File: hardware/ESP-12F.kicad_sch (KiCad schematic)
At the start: 30 parts, among them J10 PROG_PORT, U10 ESP-12F, U11 MCP2558FD-xMF, U8 PI4IOE5V6416LEX, U9 PI4IOE5V6416LEX

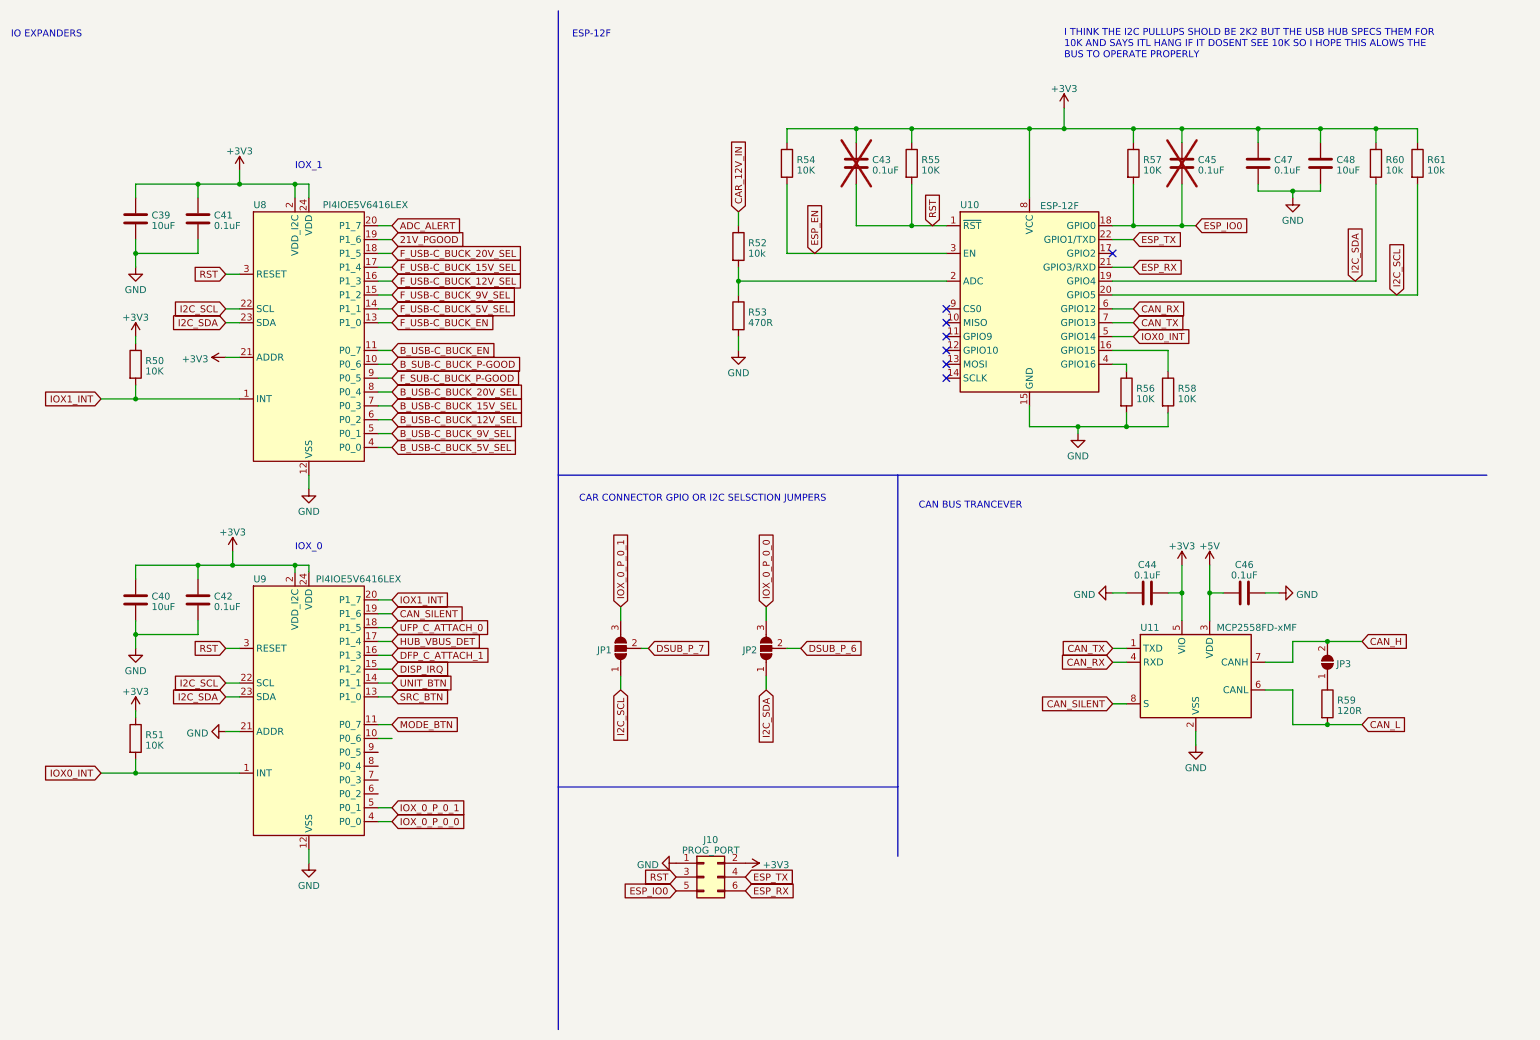
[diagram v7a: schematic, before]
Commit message: working on routing still  finnished psu section
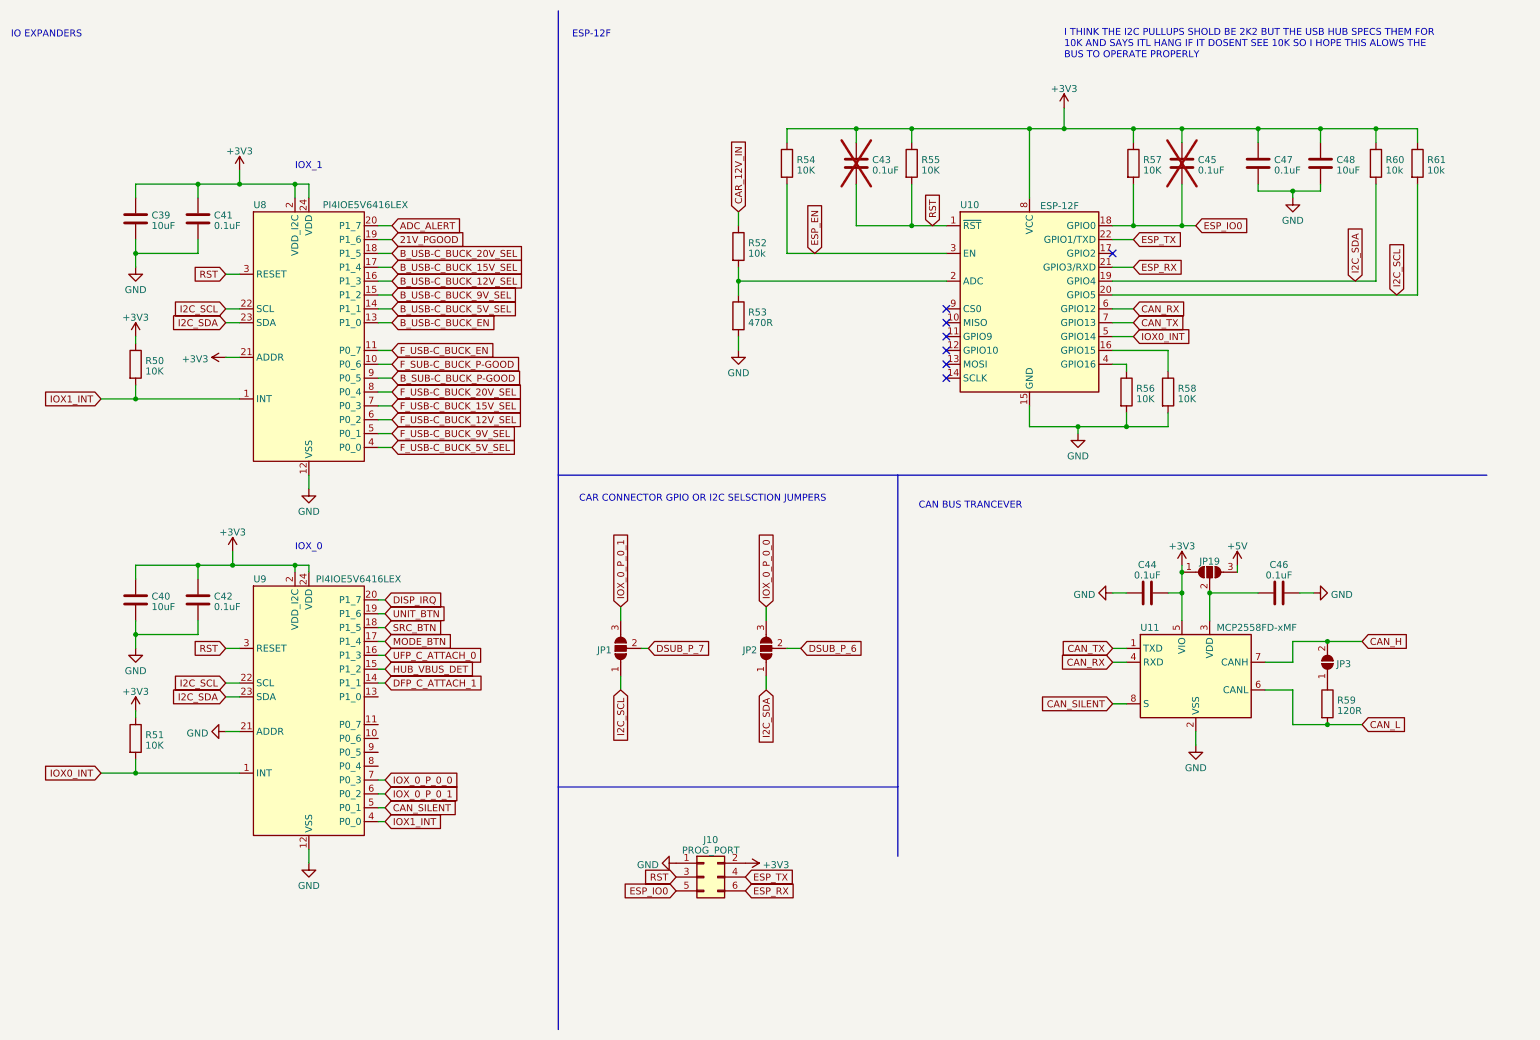
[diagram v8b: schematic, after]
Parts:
- added JP19: ~, Jumper:SolderJumper-3_P1.3mm_Open_RoundedPad1.0x1.5mm_NumberLabels, symbol Jumper:SolderJumper_3_Open
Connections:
- net +3V3: now also JP19.1 (A)
- net +5V: now also JP19.3 (B); no longer C46.1, U11.3 (VDD)
- net B_SUB-C_BUCK_P-GOOD: now also U8.9 (P0_5); no longer U8.10 (P0_6)
- net B_USB-C_BUCK_12V_SEL: now also U8.16 (P1_3); no longer U8.6 (P0_2)
- net B_USB-C_BUCK_15V_SEL: now also U8.17 (P1_4); no longer U8.7 (P0_3)
- net B_USB-C_BUCK_20V_SEL: now also U8.18 (P1_5); no longer U8.8 (P0_4)
- net B_USB-C_BUCK_5V_SEL: now also U8.14 (P1_1); no longer U8.4 (P0_0)
- net B_USB-C_BUCK_9V_SEL: now also U8.15 (P1_2); no longer U8.5 (P0_1)
- net B_USB-C_BUCK_EN: now also U8.13 (P1_0); no longer U8.11 (P0_7)
- net CAN_SILENT: now also U9.5 (P0_1); no longer U9.19 (P1_6)
- net DFP_C_ATTACH_1: now also U9.14 (P1_1); no longer U9.16 (P1_3)
- net DISP_IRQ: now also U9.20 (P1_7); no longer U9.15 (P1_2)
- net F_SUB-C_BUCK_P-GOOD: now also U8.10 (P0_6); no longer U8.9 (P0_5)
- net F_USB-C_BUCK_12V_SEL: now also U8.6 (P0_2); no longer U8.16 (P1_3)
- net F_USB-C_BUCK_15V_SEL: now also U8.7 (P0_3); no longer U8.17 (P1_4)
- net F_USB-C_BUCK_20V_SEL: now also U8.8 (P0_4); no longer U8.18 (P1_5)
- net F_USB-C_BUCK_5V_SEL: now also U8.4 (P0_0); no longer U8.14 (P1_1)
- net F_USB-C_BUCK_9V_SEL: now also U8.5 (P0_1); no longer U8.15 (P1_2)
- net F_USB-C_BUCK_EN: now also U8.11 (P0_7); no longer U8.13 (P1_0)
- net HUB_VBUS_DET: now also U9.15 (P1_2); no longer U9.17 (P1_4)
- net IOX1_INT: now also U9.4 (P0_0); no longer U9.20 (P1_7)
- net IOX_0_P_0_0: now also U9.7 (P0_3); no longer U9.4 (P0_0)
- net IOX_0_P_0_1: now also U9.6 (P0_2); no longer U9.5 (P0_1)
- net MODE_BTN: now also U9.17 (P1_4); no longer U9.11 (P0_7)
- net SRC_BTN: now also U9.18 (P1_5); no longer U9.13 (P1_0)
- net UFP_C_ATTACH_0: now also U9.16 (P1_3); no longer U9.18 (P1_5)
- net UNIT_BTN: now also U9.19 (P1_6); no longer U9.14 (P1_1)
- new net: C46.1, JP19.2 (C), U11.3 (VDD)
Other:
- moved on the sheet: C46
